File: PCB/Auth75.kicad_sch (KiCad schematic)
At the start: 209 parts, among them CN1 S2B-PH-SM4-TB, Q1 MMBT3904LT1G, Q2 MMBT3904LT1G, Q3 MMBT3904LT1G, Q4 MMBT3906LT1G, Q5 FS8205A_C2830320, SW1 EC11E15244G1, U1 RASPBERRY PI PICO 2W, U2 SL2.1S, U3 DW01A_C351410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

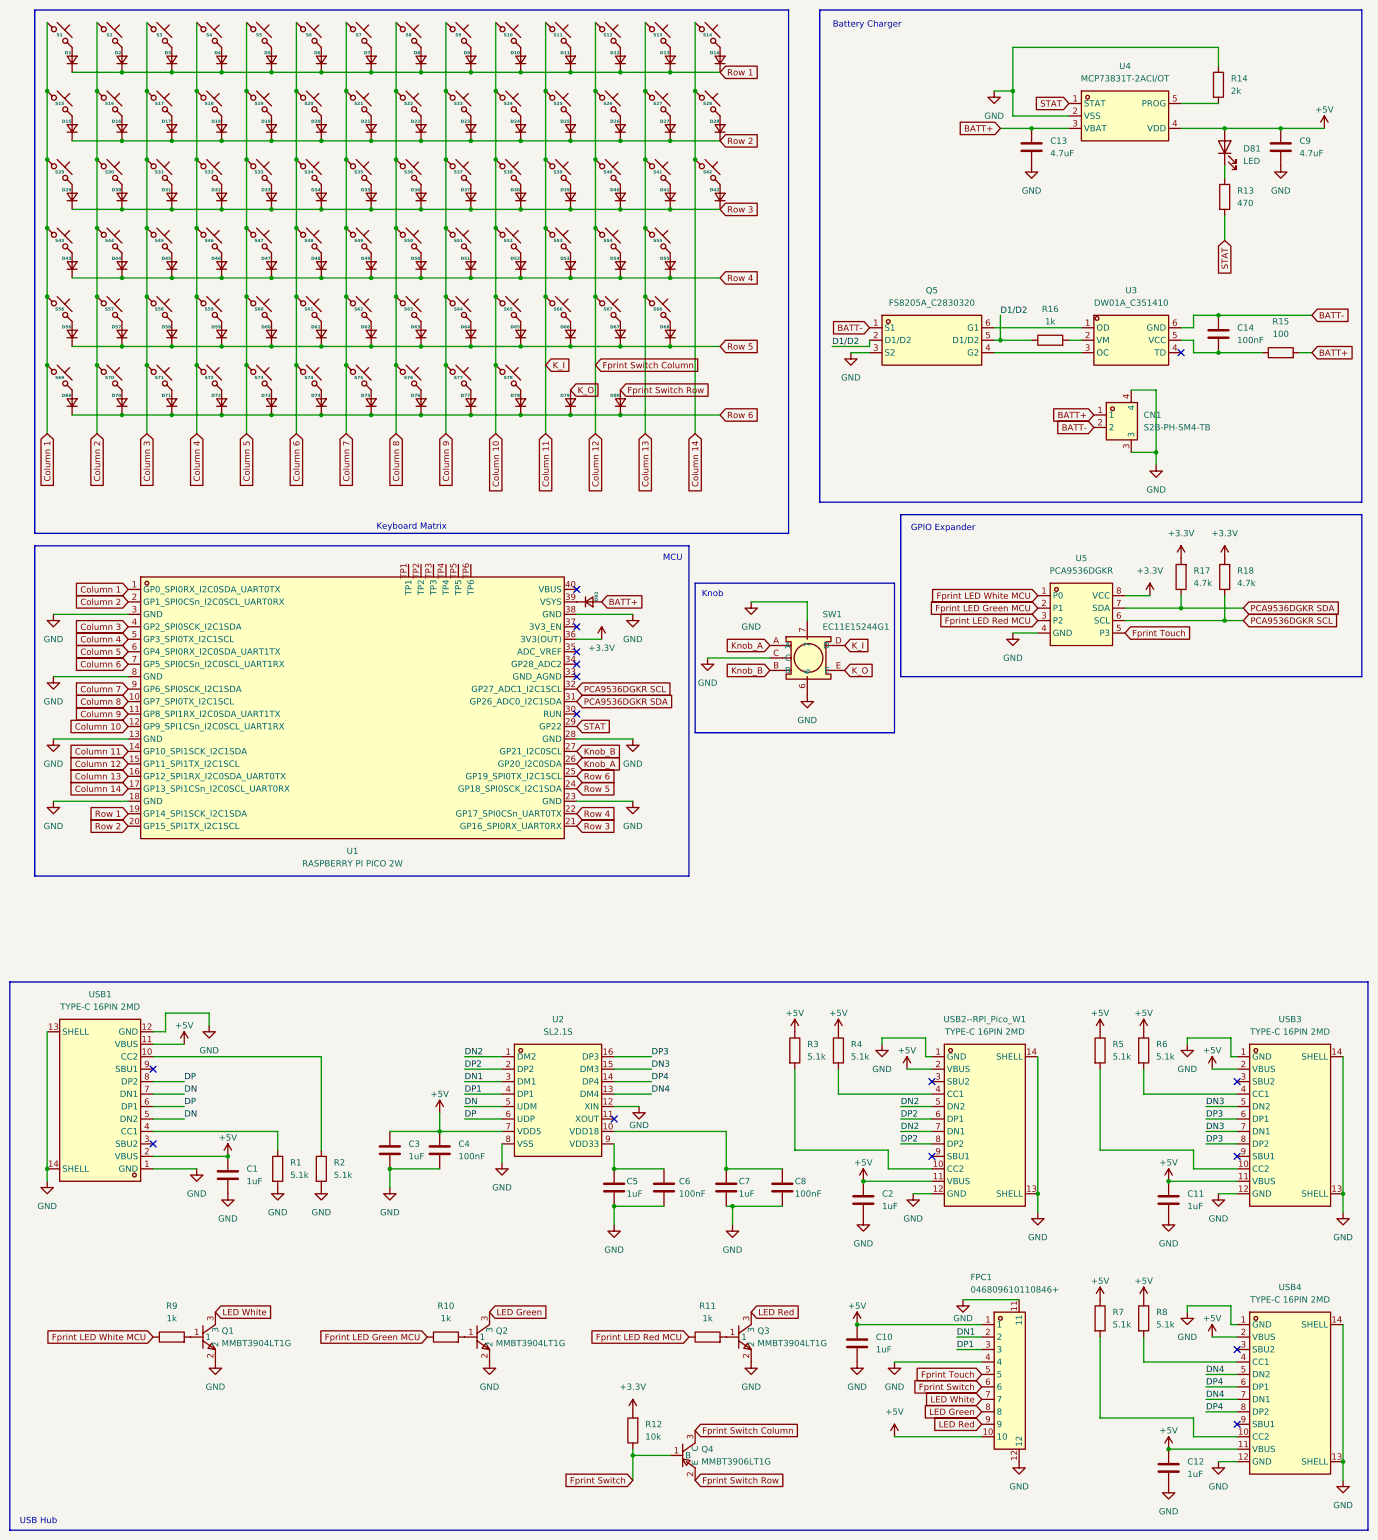
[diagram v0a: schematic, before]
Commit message: optimizing for PCBA, so it does cost too much, especially the 'Feeders loading Fee'
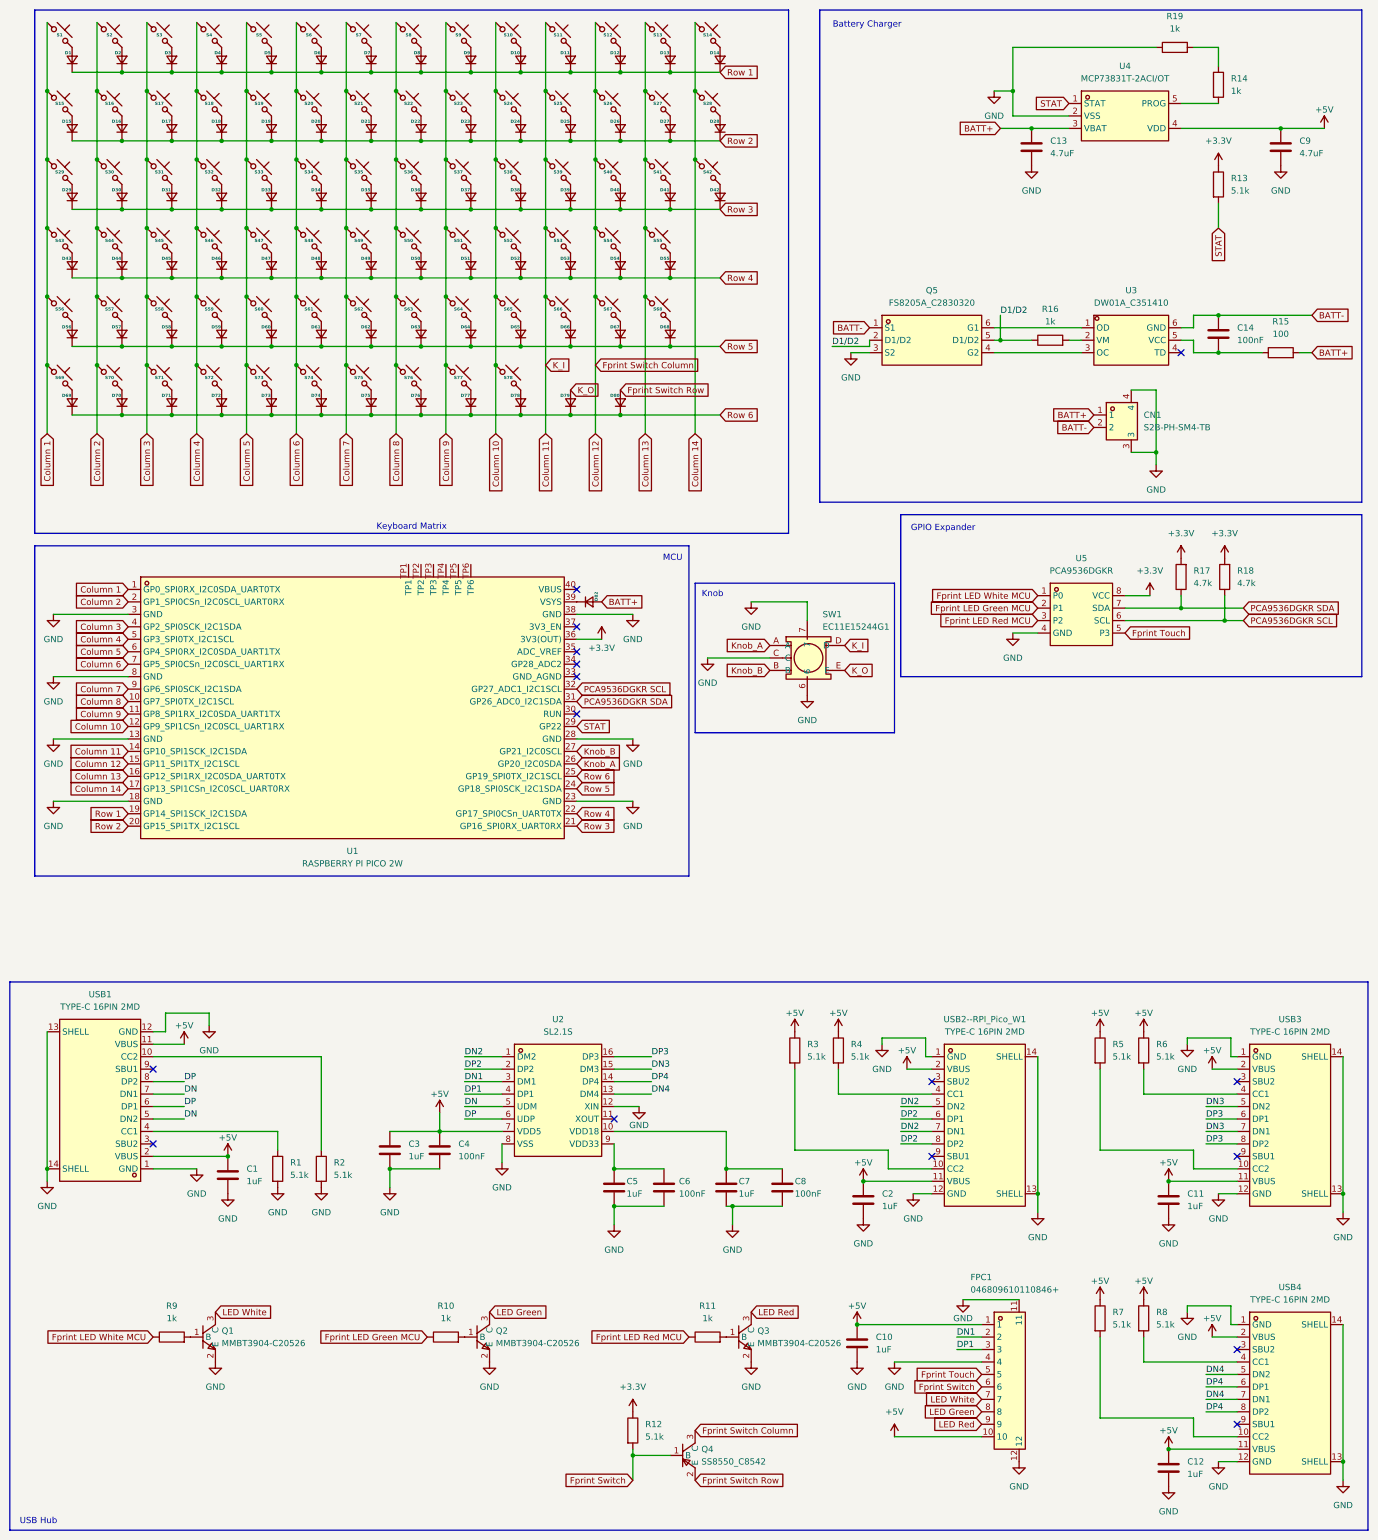
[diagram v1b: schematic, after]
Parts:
- removed D81: LED, LED_SMD:LED_0603_1608Metric, symbol Device:LED
- removed Q1, Q2, Q3: MMBT3904LT1G, easyeda2kicad:SOT-23-3_L2.9-W1.6-P1.90-LS2.8-BR, symbol easyeda2kicad:MMBT3904LT1G
- removed Q4: MMBT3906LT1G, easyeda2kicad:SOT-23-3_L2.9-W1.3-P1.90-LS2.4-BR, symbol easyeda2kicad:MMBT3906LT1G
- added Q1, Q2, Q3: MMBT3904-C20526, easyeda2kicad:SOT-23-3_L2.9-W1.3-P1.90-LS2.4-BR, symbol easyeda2kicad:MMBT3904-C20526
- added Q4: SS8550_C8542, easyeda2kicad:SOT-23-3_L2.9-W1.3-P1.90-LS2.4-BR, symbol easyeda2kicad:SS8550_C8542
- added R19: 1k, Resistor_SMD:R_0603_1608Metric, symbol Device:R
- D82: LCSC Part C169540 -> C81598
- R12: value 10k -> 5.1k; LCSC Part C25804 -> C23186
- R13: value 470 -> 5.1k; LCSC Part C23179 -> C23186
- R14: value 2k -> 1k; LCSC Part C22975 -> C21190
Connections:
- net +3.3V: now also R12.1, R13.1; no longer R12.2
- net Column 12: now also Q4.3 (C)
- net Fprint Switch: now also R12.2, Q4.1 (B); no longer R12.1
- net Fprint Switch Row: now also Q4.2 (E)
- net GND: now also Q1.2 (E), Q2.2 (E), Q3.2 (E), R19.1; no longer R14.1
- net LED Green: now also Q2.3 (C)
- net LED Red: now also Q3.3 (C)
- net LED White: now also Q1.3 (C)
- net at R10.2: now also Q2.1 (B)
- net at R11.2: now also Q3.1 (B)
- net at R9.2: now also Q1.1 (B)
- new net: R14.1, R19.2
